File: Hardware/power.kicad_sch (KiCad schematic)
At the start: 14 parts, among them J1 I2C Debug, J2 I2C, J3 I2C, U7 AP7312-1833W6-7

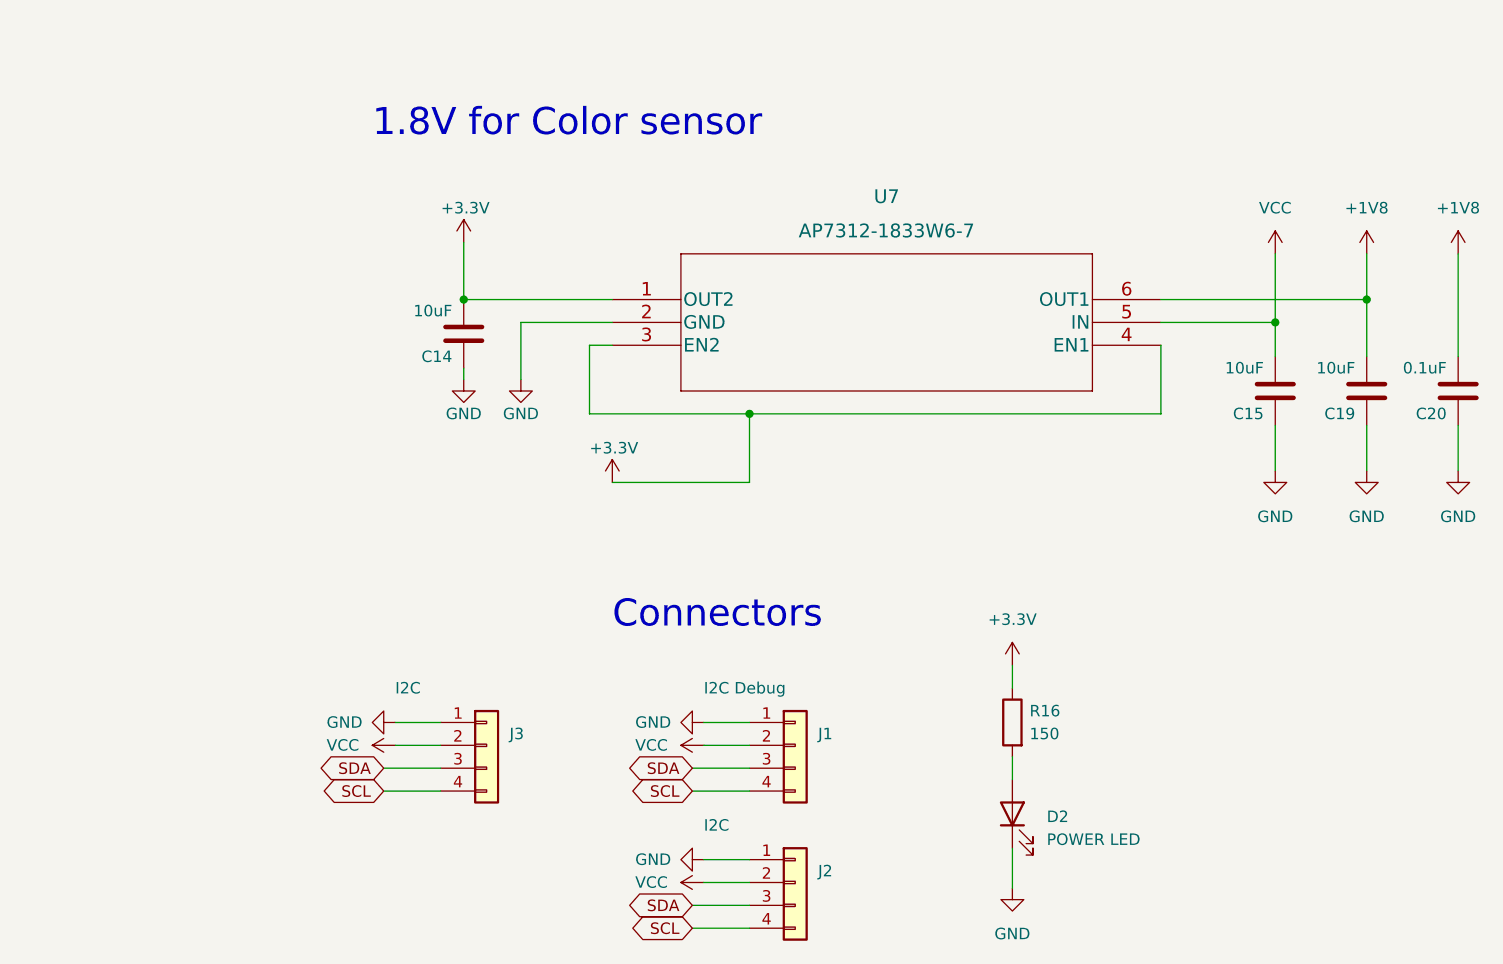
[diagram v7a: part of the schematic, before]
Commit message: in the absence of design docs, I just did my own thing.  I've kept the ribbon cable, but I am not sure why there are one on either side, I've also brought out most of the interrupt lines on the through hole headers, the headers are designed for placement on a carrier board, negating the need for the ribbon cable when the board is stacked
Signed-off-by: lokimetasmith <lokimail@gmail.com>
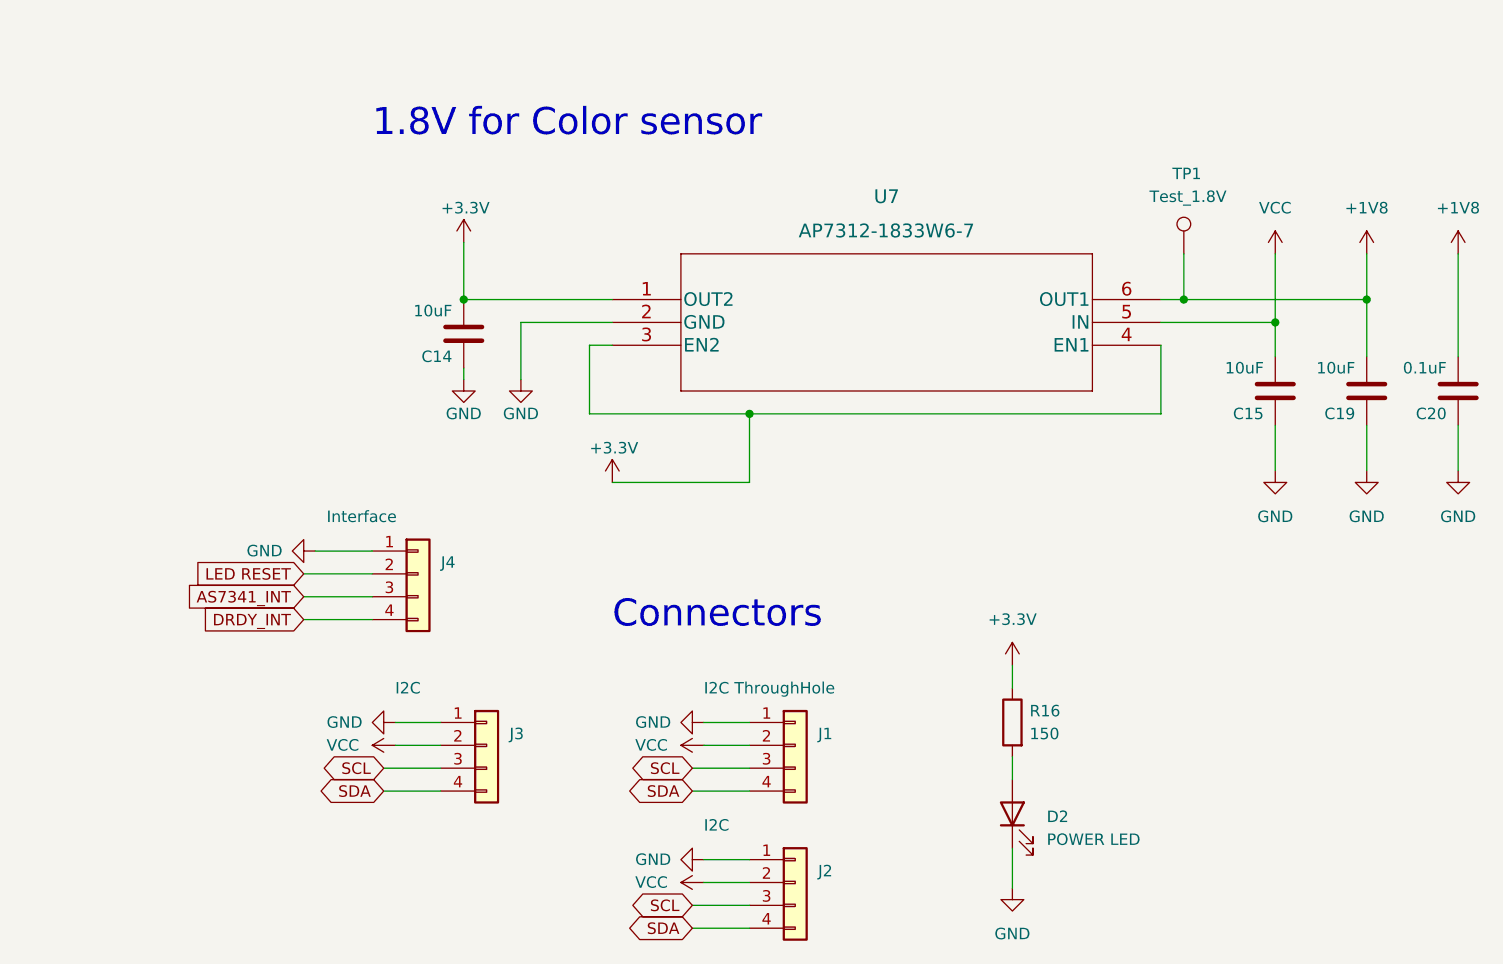
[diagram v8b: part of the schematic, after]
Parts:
- added J4: Interface, Connector_PinSocket_2.54mm:PinSocket_1x04_P2.54mm_Vertical, symbol Connector_Generic:Conn_01x04
- added TP1: Test_1.8V, TestPoint:TestPoint_Pad_D1.5mm, symbol Connector:TestPoint
- J1: value I2C Debug -> I2C ThroughHole
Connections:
- net +1V8: now also TP1.1
- net GND: now also J4.1 (Pin_1)
- net SCL: now also J1.3 (Pin_3), J2.3 (Pin_3), J3.3 (Pin_3); no longer J1.4 (Pin_4), J2.4 (Pin_4), J3.4 (Pin_4)
- net SDA: now also J1.4 (Pin_4), J2.4 (Pin_4), J3.4 (Pin_4); no longer J1.3 (Pin_3), J2.3 (Pin_3), J3.3 (Pin_3)
- new net AS7341_INT: J4.3 (Pin_3)
- new net DRDY_INT: J4.4 (Pin_4)
- new net LED RESET: J4.2 (Pin_2)
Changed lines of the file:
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@@
   (junction (at 250.19 92.71) (diameter 0) (color 0 0 0 0)
   )
+  (junction (at 240.03 90.17) (diameter 0) (color 0 0 0 0)
+  )
   (junction (at 58.42 76.2) (diameter 0) (color 0 0 0 0)
   )
@@
     (stroke (width 0) (type default) (color 0 0 0 0))
   )
+  (wire (pts (xy 142.24 120.65) (xy 149.86 120.65))
+    (stroke (width 0) (type default) (color 0 0 0 0))
+  )
   (wire (pts (xy 220.98 151.13) (xy 220.98 155.575))
     (stroke (width 0) (type default) (color 0 0 0 0))
@@
     (stroke (width 0) (type default) (color 0 0 0 0))
   )
+  (wire (pts (xy 240.03 85.09) (xy 240.03 90.17))
+    (stroke (width 0) (type default) (color 0 0 0 0))
+  )
   (wire (pts (xy 220.98 140.97) (xy 220.98 143.51))
     (stroke (width 0) (type default) (color 0 0 0 0))
@@
     (stroke (width 0) (type default) (color 0 0 0 0))
   )
-  (wire (pts (xy 237.49 90.17) (xy 260.35 90.17))
+  (wire (pts (xy 237.49 90.17) (xy 240.03 90.17))
     (stroke (width 0) (type default) (color 0 0 0 0))
   )
@@
     (stroke (width 0) (type default) (color 0 0 0 0))
   )
+  (wire (pts (xy 142.24 125.73) (xy 149.86 125.73))
+    (stroke (width 0) (type default) (color 0 0 0 0))
+  )
   (wire (pts (xy 166.37 92.71) (xy 166.37 99.06))
     (stroke (width 0) (type default) (color 0 0 0 0))
@@
     (stroke (width 0) (type default) (color 0 0 0 0))
   )
+  (wire (pts (xy 143.51 118.11) (xy 149.86 118.11))
+    (stroke (width 0) (type default) (color 0 0 0 0))
+  )
+  (wire (pts (xy 142.24 123.19) (xy 149.86 123.19))
+    (stroke (width 0) (type default) (color 0 0 0 0))
+  )
   (wire (pts (xy 250.19 85.09) (xy 250.19 92.71))
     (stroke (width 0) (type default) (color 0 0 0 0))
@@
   )
   (wire (pts (xy 186.69 139.7) (xy 191.77 139.7))
+    (stroke (width 0) (type default) (color 0 0 0 0))
+  )
+  (wire (pts (xy 240.03 90.17) (xy 260.35 90.17))
     (stroke (width 0) (type default) (color 0 0 0 0))
   )
@@
     (effects (font (size 3 3)) (justify left bottom))
   )
-  (global_label "SCL" (shape bidirectional) (at 185.42 160.02 180) (fields_autoplaced)
-    (effects (font (size 1.27 1.27)) (justify right))
-    (property "Intersheet References" "${INTERSHEET_REFS}" (id 0) (at 179.4993 159.9406 0)
-      (effects (font (size 1.27 1.27)) (justify right) hide)
-    )
-  )
-  (global_label "SDA" (shape bidirectional) (at 185.42 157.48 180) (fields_autoplaced)
-    (effects (font (size 1.27 1.27)) (justify right))
-    (property "Intersheet References" "${INTERSHEET_REFS}" (id 0) (at 179.4388 157.5594 0)
-      (effects (font (size 1.27 1.27)) (justify right) hide)
-    )
-  )
-  (global_label "SDA" (shape bidirectional) (at 185.42 142.24 180) (fields_autoplaced)
-    (effects (font (size 1.27 1.27)) (justify right))
-    (property "Intersheet References" "${INTERSHEET_REFS}" (id 0) (at 179.4388 142.3194 0)
-      (effects (font (size 1.27 1.27)) (justify right) hide)
-    )
-  )
-  (global_label "SDA" (shape bidirectional) (at 151.13 142.24 180) (fields_autoplaced)
-    (effects (font (size 1.27 1.27)) (justify right))
-    (property "Intersheet References" "${INTERSHEET_REFS}" (id 0) (at 145.1488 142.3194 0)
+  (global_label "SCL" (shape bidirectional) (at 185.42 157.48 180) (fields_autoplaced)
+    (effects (font (size 1.27 1.27)) (justify right))
+    (property "Intersheet References" "${INTERSHEET_REFS}" (id 0) (at 179.4993 157.4006 0)
+      (effects (font (size 1.27 1.27)) (justify right) hide)
+    )
+  )
+  (global_label "SDA" (shape bidirectional) (at 185.42 160.02 180) (fields_autoplaced)
+    (effects (font (size 1.27 1.27)) (justify right))
+    (property "Intersheet References" "${INTERSHEET_REFS}" (id 0) (at 179.4388 160.0994 0)
+      (effects (font (size 1.27 1.27)) (justify right) hide)
+    )
+  )
+  (global_label "DRDY_INT" (shape input) (at 142.24 125.73 180) (fields_autoplaced)
+    (effects (font (size 1.27 1.27)) (justify right))
+    (property "Intersheet References" "${INTERSHEET_REFS}" (id 0) (at 131.0579 125.8094 0)
+      (effects (font (size 1.27 1.27)) (justify right) hide)
+    )
+  )
+  (global_label "SDA" (shape bidirectional) (at 185.42 144.78 180) (fields_autoplaced)
+    (effects (font (size 1.27 1.27)) (justify right))
+    (property "Intersheet References" "${INTERSHEET_REFS}" (id 0) (at 179.4388 144.8594 0)
+      (effects (font (size 1.27 1.27)) (justify right) hide)
+    )
+  )
+  (global_label "AS7341_INT" (shape input) (at 142.24 123.19 180) (fields_autoplaced)
+    (effects (font (size 1.27 1.27)) (justify right))
+    (property "Intersheet References" "${INTERSHEET_REFS}" (id 0) (at 128.8202 123.2694 0)
+      (effects (font (size 1.27 1.27)) (justify right) hide)
+    )
+  )
+  (global_label "SDA" (shape bidirectional) (at 151.13 144.78 180) (fields_autoplaced)
+    (effects (font (size 1.27 1.27)) (justify right))
+    (property "Intersheet References" "${INTERSHEET_REFS}" (id 0) (at 145.1488 144.8594 0)
       (effects (font (size 1.27 1.27)) (justify right) hide)
     )
@@
     )
   )
-  (global_label "SCL" (shape bidirectional) (at 185.42 144.78 180) (fields_autoplaced)
-    (effects (font (size 1.27 1.27)) (justify right))
-    (property "Intersheet References" "${INTERSHEET_REFS}" (id 0) (at 179.4993 144.7006 0)
+  (global_label "LED RESET" (shape input) (at 142.24 120.65 180) (fields_autoplaced)
+    (effects (font (size 1.27 1.27)) (justify right))
+    (property "Intersheet References" "${INTERSHEET_REFS}" (id 0) (at 129.6669 120.7294 0)
+      (effects (font (size 1.27 1.27)) (justify right) hide)
+    )
+  )
+  (global_label "SCL" (shape bidirectional) (at 185.42 142.24 180) (fields_autoplaced)
+    (effects (font (size 1.27 1.27)) (justify right))
+    (property "Intersheet References" "${INTERSHEET_REFS}" (id 0) (at 179.4993 142.1606 0)
       (effects (font (size 1.27 1.27)) (justify right) hide)
     )
@@
     )
   )
-  (global_label "SCL" (shape bidirectional) (at 151.13 144.78 180) (fields_autoplaced)
-    (effects (font (size 1.27 1.27)) (justify right))
-    (property "Intersheet References" "${INTERSHEET_REFS}" (id 0) (at 145.2093 144.7006 0)
+  (global_label "SCL" (shape bidirectional) (at 151.13 142.24 180) (fields_autoplaced)
+    (effects (font (size 1.27 1.27)) (justify right))
+    (property "Intersheet References" "${INTERSHEET_REFS}" (id 0) (at 145.2093 142.1606 0)
       (effects (font (size 1.27 1.27)) (justify right) hide)
     )
@@
     (pin "1")
   )
+  (symbol (lib_id "power:GND") (at 143.51 118.11 270) (unit 1)
+    (in_bom yes) (on_board yes)
+    (property "Reference" "#PWR010" (id 0) (at 137.16 118.11 0)
+      (effects (font (size 1.27 1.27)) hide)
+    )
+    (property "Value" "GND" (id 1) (at 135.89 118.11 90)
+      (effects (font (size 1.27 1.27)) (justify left))
+    )
+    (property "Footprint" "" (id 2) (at 143.51 118.11 0)
+      (effects (font (size 1.27 1.27)) hide)
+    )
+    (property "Datasheet" "" (id 3) (at 143.51 118.11 0)
+      (effects (font (size 1.27 1.27)) hide)
+    )
+    (pin "1")
+  )
   (symbol (lib_id "power:GND") (at 220.98 155.575 0) (unit 1)
     (in_bom yes) (on_board yes) (fields_autoplaced)
@@
     (pin "1")
   )
+  (symbol (lib_id "Connector:TestPoint") (at 240.03 85.09 0) (unit 1)
+    (in_bom yes) (on_board yes)
+    (property "Reference" "TP1" (id 0) (at 238.76 76.2 0)
+      (effects (font (size 1.27 1.27)) (justify left))
+    )
+    (property "Value" "Test_1.8V" (id 1) (at 236.22 78.74 0)
+      (effects (font (size 1.27 1.27)) (justify left))
+    )
+    (property "Footprint" "TestPoint:TestPoint_Pad_D1.5mm" (id 2) (at 245.11 85.09 0)
+      (effects (font (size 1.27 1.27)) hide)
+    )
+    (property "Datasheet" "~" (id 3) (at 245.11 85.09 0)
+      (effects (font (size 1.27 1.27)) hide)
+    )
+    (pin "1")
+  )
   (symbol (lib_id "Device:LED") (at 220.98 147.32 90) (unit 1)
     (in_bom yes) (on_board yes) (fields_autoplaced)
@@
     (pin "2")
   )
+  (symbol (lib_id "Connector_Generic:Conn_01x04") (at 154.94 120.65 0) (unit 1)
+    (in_bom yes) (on_board yes)
+    (property "Reference" "J4" (id 0) (at 157.48 119.3799 0)
+      (effects (font (size 1.27 1.27)) (justify left))
+    )
+    (property "Value" "Interface" (id 1) (at 144.78 114.3 0)
+      (effects (font (size 1.27 1.27)) (justify left))
+    )
+    (property "Footprint" "Connector_PinSocket_2.54mm:PinSocket_1x04_P2.54mm_Vertical" (id 2) (at 154.94 120.65 0)
+      (effects (font (size 1.27 1.27)) hide)
+    )
+    (property "Datasheet" "~" (id 3) (at 154.94 120.65 0)
+      (effects (font (size 1.27 1.27)) hide)
+    )
+    (pin "1")
+    (pin "2")
+    (pin "3")
+    (pin "4")
+  )
   (symbol (lib_id "Connector_Generic:Conn_01x04") (at 196.85 139.7 0) (unit 1)
     (in_bom yes) (on_board yes)
@@
       (effects (font (size 1.27 1.27)) (justify left))
     )
-    (property "Value" "I2C Debug" (id 1) (at 186.69 133.35 0)
-      (effects (font (size 1.27 1.27)) (justify left))
-    )
+    (property "Value" "I2C ThroughHole" (id 1) (at 186.69 133.35 0)
+      (effects (font (size 1.27 1.27)) (justify left))
+    )
